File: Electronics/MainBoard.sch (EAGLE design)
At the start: 10 parts, among them J1 1X2-3.5MM

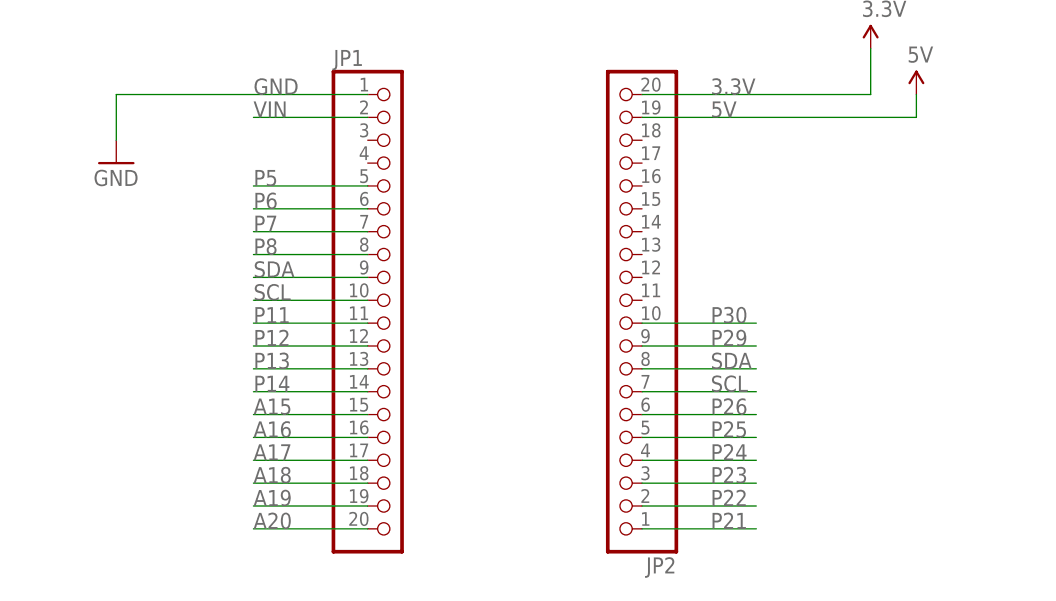
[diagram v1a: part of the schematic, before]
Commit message: half routed
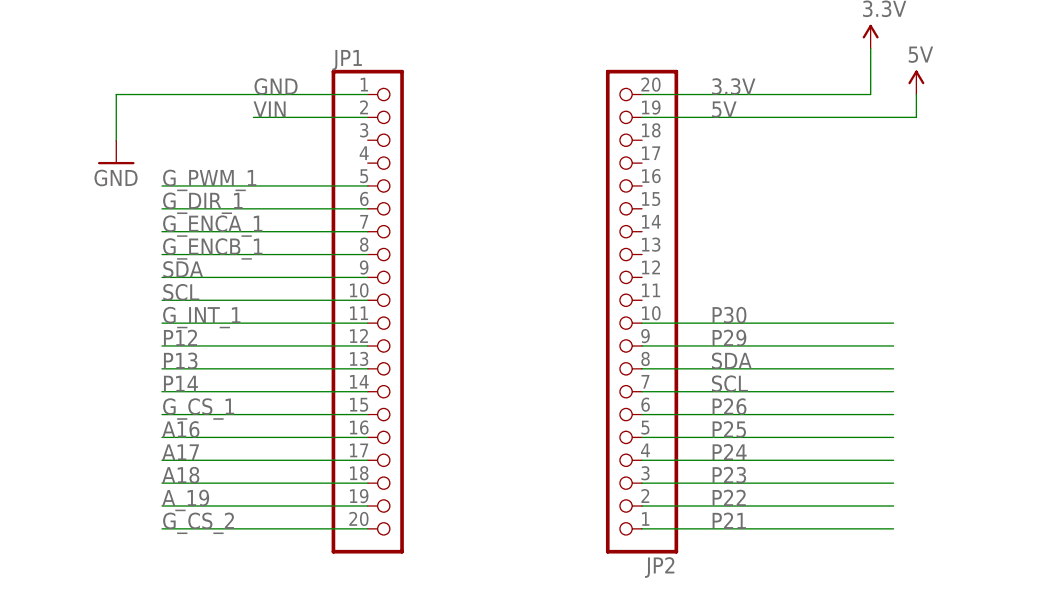
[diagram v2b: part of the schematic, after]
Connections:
- net A19 renamed A_19
- removed net A15: JP1.15
- removed net A20: JP1.20
- removed net P11: JP1.11
- removed net P5: JP1.5
- removed net P6: JP1.6
- removed net P7: JP1.7
- removed net P8: JP1.8
- net G_CS_1: now also JP1.15
- net G_CS_2: now also JP1.20
- net G_DIR_1: now also JP1.6
- net G_ENCA_1: now also JP1.7
- net G_ENCB_1: now also JP1.8
- net G_INT_1: now also JP1.11
- net G_PWM_1: now also JP1.5
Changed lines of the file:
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@@
 <segment>
 <pinref part="JP2" gate="A" pin="7"/>
-<wire x1="45.72" y1="73.66" x2="58.42" y2="73.66" width="0.1524" layer="91"/>
+<wire x1="45.72" y1="73.66" x2="73.66" y2="73.66" width="0.1524" layer="91"/>
 <label x="53.34" y="73.66" size="1.778" layer="95"/>
 </segment>
 <segment>
 <pinref part="JP1" gate="A" pin="10"/>
-<wire x1="15.24" y1="83.82" x2="2.54" y2="83.82" width="0.1524" layer="91"/>
-<label x="2.54" y="83.82" size="1.778" layer="95"/>
+<wire x1="15.24" y1="83.82" x2="-7.62" y2="83.82" width="0.1524" layer="91"/>
+<label x="-7.62" y="83.82" size="1.778" layer="95"/>
 </segment>
 <segment>
@@
 <segment>
 <pinref part="JP2" gate="A" pin="8"/>
-<wire x1="45.72" y1="76.2" x2="58.42" y2="76.2" width="0.1524" layer="91"/>
+<wire x1="45.72" y1="76.2" x2="73.66" y2="76.2" width="0.1524" layer="91"/>
 <label x="53.34" y="76.2" size="1.778" layer="95"/>
 </segment>
 <segment>
 <pinref part="JP1" gate="A" pin="9"/>
-<wire x1="15.24" y1="86.36" x2="2.54" y2="86.36" width="0.1524" layer="91"/>
-<label x="2.54" y="86.36" size="1.778" layer="95"/>
+<wire x1="15.24" y1="86.36" x2="-7.62" y2="86.36" width="0.1524" layer="91"/>
+<label x="-7.62" y="86.36" size="1.778" layer="95"/>
 </segment>
 <segment>
@@
 <segment>
 <pinref part="JP2" gate="A" pin="10"/>
-<wire x1="45.72" y1="81.28" x2="58.42" y2="81.28" width="0.1524" layer="91"/>
+<wire x1="45.72" y1="81.28" x2="73.66" y2="81.28" width="0.1524" layer="91"/>
 <label x="53.34" y="81.28" size="1.778" layer="95"/>
 </segment>
@@
 <segment>
 <pinref part="JP2" gate="A" pin="9"/>
-<wire x1="45.72" y1="78.74" x2="58.42" y2="78.74" width="0.1524" layer="91"/>
+<wire x1="45.72" y1="78.74" x2="73.66" y2="78.74" width="0.1524" layer="91"/>
 <label x="53.34" y="78.74" size="1.778" layer="95"/>
 </segment>
@@
 <segment>
 <pinref part="JP2" gate="A" pin="6"/>
-<wire x1="45.72" y1="71.12" x2="58.42" y2="71.12" width="0.1524" layer="91"/>
+<wire x1="45.72" y1="71.12" x2="73.66" y2="71.12" width="0.1524" layer="91"/>
 <label x="53.34" y="71.12" size="1.778" layer="95"/>
 </segment>
@@
 <segment>
 <pinref part="JP2" gate="A" pin="5"/>
-<wire x1="45.72" y1="68.58" x2="58.42" y2="68.58" width="0.1524" layer="91"/>
+<wire x1="45.72" y1="68.58" x2="73.66" y2="68.58" width="0.1524" layer="91"/>
 <label x="53.34" y="68.58" size="1.778" layer="95"/>
 </segment>
@@
 <segment>
 <pinref part="JP2" gate="A" pin="4"/>
-<wire x1="45.72" y1="66.04" x2="58.42" y2="66.04" width="0.1524" layer="91"/>
+<wire x1="45.72" y1="66.04" x2="73.66" y2="66.04" width="0.1524" layer="91"/>
 <label x="53.34" y="66.04" size="1.778" layer="95"/>
 </segment>
@@
 <segment>
 <pinref part="JP2" gate="A" pin="2"/>
-<wire x1="45.72" y1="60.96" x2="58.42" y2="60.96" width="0.1524" layer="91"/>
+<wire x1="45.72" y1="60.96" x2="73.66" y2="60.96" width="0.1524" layer="91"/>
 <label x="53.34" y="60.96" size="1.778" layer="95"/>
 </segment>
@@
 <segment>
 <pinref part="JP2" gate="A" pin="1"/>
-<wire x1="45.72" y1="58.42" x2="58.42" y2="58.42" width="0.1524" layer="91"/>
+<wire x1="45.72" y1="58.42" x2="73.66" y2="58.42" width="0.1524" layer="91"/>
 <label x="53.34" y="58.42" size="1.778" layer="95"/>
 </segment>
 </net>
-<net name="P5" class="0">
-<segment>
-<pinref part="JP1" gate="A" pin="5"/>
-<wire x1="15.24" y1="96.52" x2="2.54" y2="96.52" width="0.1524" layer="91"/>
-<label x="2.54" y="96.52" size="1.778" layer="95"/>
-</segment>
-</net>
-<net name="P6" class="0">
-<segment>
-<pinref part="JP1" gate="A" pin="6"/>
-<wire x1="15.24" y1="93.98" x2="2.54" y2="93.98" width="0.1524" layer="91"/>
-<label x="2.54" y="93.98" size="1.778" layer="95"/>
-</segment>
-</net>
-<net name="P7" class="0">
-<segment>
-<pinref part="JP1" gate="A" pin="7"/>
-<wire x1="15.24" y1="91.44" x2="2.54" y2="91.44" width="0.1524" layer="91"/>
-<label x="2.54" y="91.44" size="1.778" layer="95"/>
-</segment>
-</net>
-<net name="P8" class="0">
-<segment>
-<pinref part="JP1" gate="A" pin="8"/>
-<wire x1="15.24" y1="88.9" x2="2.54" y2="88.9" width="0.1524" layer="91"/>
-<label x="2.54" y="88.9" size="1.778" layer="95"/>
-</segment>
-</net>
-<net name="P11" class="0">
-<segment>
-<pinref part="JP1" gate="A" pin="11"/>
-<wire x1="15.24" y1="81.28" x2="2.54" y2="81.28" width="0.1524" layer="91"/>
-<label x="2.54" y="81.28" size="1.778" layer="95"/>
-</segment>
-</net>
 <net name="P12" class="0">
 <segment>
 <pinref part="JP1" gate="A" pin="12"/>
-<wire x1="15.24" y1="78.74" x2="2.54" y2="78.74" width="0.1524" layer="91"/>
-<label x="2.54" y="78.74" size="1.778" layer="95"/>
+<wire x1="15.24" y1="78.74" x2="-7.62" y2="78.74" width="0.1524" layer="91"/>
+<label x="-7.62" y="78.74" size="1.778" layer="95"/>
 </segment>
 </net>
@@
 <segment>
 <pinref part="JP1" gate="A" pin="13"/>
-<wire x1="15.24" y1="76.2" x2="2.54" y2="76.2" width="0.1524" layer="91"/>
-<label x="2.54" y="76.2" size="1.778" layer="95"/>
+<wire x1="15.24" y1="76.2" x2="-7.62" y2="76.2" width="0.1524" layer="91"/>
+<label x="-7.62" y="76.2" size="1.778" layer="95"/>
 </segment>
 </net>
@@
 <segment>
 <pinref part="JP1" gate="A" pin="14"/>
-<wire x1="15.24" y1="73.66" x2="2.54" y2="73.66" width="0.1524" layer="91"/>
-<label x="2.54" y="73.66" size="1.778" layer="95"/>
-</segment>
-</net>
-<net name="A15" class="0">
-<segment>
-<pinref part="JP1" gate="A" pin="15"/>
-<wire x1="15.24" y1="71.12" x2="2.54" y2="71.12" width="0.1524" layer="91"/>
-<label x="2.54" y="71.12" size="1.778" layer="95"/>
+<wire x1="15.24" y1="73.66" x2="-7.62" y2="73.66" width="0.1524" layer="91"/>
+<label x="-7.62" y="73.66" size="1.778" layer="95"/>
 </segment>
 </net>
@@
 <segment>
 <pinref part="JP1" gate="A" pin="16"/>
-<wire x1="15.24" y1="68.58" x2="2.54" y2="68.58" width="0.1524" layer="91"/>
-<label x="2.54" y="68.58" size="1.778" layer="95"/>
+<wire x1="15.24" y1="68.58" x2="-7.62" y2="68.58" width="0.1524" layer="91"/>
+<label x="-7.62" y="68.58" size="1.778" layer="95"/>
 </segment>
 </net>
@@
 <segment>
 <pinref part="JP1" gate="A" pin="18"/>
-<wire x1="15.24" y1="63.5" x2="2.54" y2="63.5" width="0.1524" layer="91"/>
-<label x="2.54" y="63.5" size="1.778" layer="95"/>
-</segment>
-</net>
-<net name="A19" class="0">
-<segment>
-<pinref part="JP1" gate="A" pin="19"/>
-<wire x1="15.24" y1="60.96" x2="2.54" y2="60.96" width="0.1524" layer="91"/>
-<label x="2.54" y="60.96" size="1.778" layer="95"/>
-</segment>
-</net>
-<net name="A20" class="0">
-<segment>
-<pinref part="JP1" gate="A" pin="20"/>
-<wire x1="15.24" y1="58.42" x2="2.54" y2="58.42" width="0.1524" layer="91"/>
-<label x="2.54" y="58.42" size="1.778" layer="95"/>
+<wire x1="15.24" y1="63.5" x2="-7.62" y2="63.5" width="0.1524" layer="91"/>
+<label x="-7.62" y="63.5" size="1.778" layer="95"/>
 </segment>
 </net>
@@
 <segment>
 <pinref part="JP2" gate="A" pin="3"/>
-<wire x1="45.72" y1="63.5" x2="58.42" y2="63.5" width="0.1524" layer="91"/>
+<wire x1="45.72" y1="63.5" x2="73.66" y2="63.5" width="0.1524" layer="91"/>
 <label x="53.34" y="63.5" size="1.778" layer="95"/>
 </segment>
@@
 <segment>
 <pinref part="JP1" gate="A" pin="17"/>
-<wire x1="15.24" y1="66.04" x2="2.54" y2="66.04" width="0.1524" layer="91"/>
-<label x="2.54" y="66.04" size="1.778" layer="95"/>
+<wire x1="15.24" y1="66.04" x2="-7.62" y2="66.04" width="0.1524" layer="91"/>
+<label x="-7.62" y="66.04" size="1.778" layer="95"/>
 </segment>
 </net>
@@
 <label x="101.6" y="127" size="1.778" layer="95"/>
 </segment>
+<segment>
+<pinref part="JP1" gate="A" pin="5"/>
+<wire x1="15.24" y1="96.52" x2="-7.62" y2="96.52" width="0.1524" layer="91"/>
+<label x="-7.62" y="96.52" size="1.778" layer="95"/>
+</segment>
 </net>
 <net name="G_DIR_1" class="0">
@@
 <label x="101.6" y="124.46" size="1.778" layer="95"/>
 </segment>
+<segment>
+<pinref part="JP1" gate="A" pin="6"/>
+<wire x1="15.24" y1="93.98" x2="-7.62" y2="93.98" width="0.1524" layer="91"/>
+<label x="-7.62" y="93.98" size="1.778" layer="95"/>
+</segment>
 </net>
 <net name="G_ENCA_1" class="0">
@@
 <label x="101.6" y="121.92" size="1.778" layer="95"/>
 </segment>
+<segment>
+<pinref part="JP1" gate="A" pin="7"/>
+<wire x1="15.24" y1="91.44" x2="-7.62" y2="91.44" width="0.1524" layer="91"/>
+<label x="-7.62" y="91.44" size="1.778" layer="95"/>
+</segment>
 </net>
 <net name="G_ENCB_1" class="0">
@@
 <label x="101.6" y="119.38" size="1.778" layer="95"/>
 </segment>
+<segment>
+<pinref part="JP1" gate="A" pin="8"/>
+<wire x1="15.24" y1="88.9" x2="-7.62" y2="88.9" width="0.1524" layer="91"/>
+<label x="-7.62" y="88.9" size="1.778" layer="95"/>
+</segment>
 </net>
 <net name="G_INT_1" class="0">
@@
 <label x="101.6" y="109.22" size="1.778" layer="95"/>
 </segment>
+<segment>
+<pinref part="JP1" gate="A" pin="11"/>
+<wire x1="15.24" y1="81.28" x2="-7.62" y2="81.28" width="0.1524" layer="91"/>
+<label x="-7.62" y="81.28" size="1.778" layer="95"/>
+</segment>
 </net>
 <net name="G_CS_1" class="0">
@@
 <wire x1="119.38" y1="104.14" x2="101.6" y2="104.14" width="0.1524" layer="91"/>
 <label x="101.6" y="104.14" size="1.778" layer="95"/>
+</segment>
+<segment>
+<pinref part="JP1" gate="A" pin="15"/>
+<wire x1="15.24" y1="71.12" x2="-7.62" y2="71.12" width="0.1524" layer="91"/>
+<label x="-7.62" y="71.12" size="1.778" layer="95"/>
 </segment>
 </net>
@@
 <label x="48.26" y="144.78" size="1.778" layer="95"/>
 </segment>
+<segment>
+<pinref part="JP1" gate="A" pin="20"/>
+<wire x1="15.24" y1="58.42" x2="-7.62" y2="58.42" width="0.1524" layer="91"/>
+<label x="-7.62" y="58.42" size="1.778" layer="95"/>
+</segment>
 </net>
 <net name="MOT_ENC_A" class="0">
@@
 </segment>
 </net>
+<net name="A_19" class="0">
+<segment>
+<pinref part="JP1" gate="A" pin="19"/>
+<wire x1="15.24" y1="60.96" x2="-7.62" y2="60.96" width="0.1524" layer="91"/>
+<label x="-7.62" y="60.96" size="1.778" layer="95"/>
+</segment>
+</net>
